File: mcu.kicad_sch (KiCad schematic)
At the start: 61 parts, among them J10 Micro_SD_Card, J11 Conn_01x06, J12 Conn_01x02, J13 USB_B, J14 USB_B, J8 Conn_02x05_Odd_Even, J9 Conn_01x06, SW1 SW_Push, SW2 SW_Push, U24 REF3333, U25 LPS25HB, U26 STM32F427ZGTx, U27 USBLC6-2SC6, Y1 8MHz

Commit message: update
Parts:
- removed J13: USB_B, conn_5_2.5mm:conn_5_2.5mm, symbol Connector_Generic:Conn_01x05
- removed J9: Conn_01x06, Connector:Tag-Connect_TC2030-IDC-NL_2x03_P1.27mm_Vertical, symbol Connector_Generic:Conn_01x06
- J12: footprint Connector_PinHeader_2.54mm:PinHeader_1x02_P2.54mm_Vertical -> Connector_PinHeader_2.54mm:PinHeader_1x04_P2.54mm_Vertical; symbol Connector_Generic:Conn_01x02 -> Connector_Generic:Conn_01x04
- J8: footprint Connector_PinHeader_1.27mm:PinHeader_2x05_P1.27mm_Vertical_SMD -> Connector_PinHeader_2.54mm:PinHeader_2x05_P2.54mm_Vertical
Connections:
- net +3V3: now also J12.1 (Pin_1)
- net GND: now also J12.4 (Pin_4)
- net UART_RX: now also J12.3 (Pin_3); no longer J12.2 (Pin_2)
- net UART_TX: now also J12.2 (Pin_2); no longer J12.1 (Pin_1)
- net AV10: now reaches U26.41 (PA5)
- net AV11: now reaches U26.42 (PA6)
- net AT3: now reaches U26.46 (PB0)
- net AT4: now reaches U26.47 (PB1)
- net LS17: now reaches U26.56 (PG0)
- net LS18: now reaches U26.57 (PG1)
- no-connect marks 31 -> 30
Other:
- note added: "1.3V @ 12V"
- note removed: "Pin header"
- note removed: "Tag Connect Debug Header"

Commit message: Updates - Route digital inputs to connector - Add optional VR conditioner - Second Enable for H-Bridge
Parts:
- D12, D13, D14, D15, D16: footprint LED_SMD:LED_0603_1608Metric_Castellated -> LED_SMD:LED_0603_1608Metric
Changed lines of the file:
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@@
       (effects (font (size 1.27 1.27)))
     )
-    (property "Footprint" "LED_SMD:LED_0603_1608Metric_Castellated" (at 211.455 173.99 0)
+    (property "Footprint" "LED_SMD:LED_0603_1608Metric" (at 211.455 173.99 0)
       (effects (font (size 1.27 1.27)) hide)
     )
@@
       (effects (font (size 1.27 1.27)))
     )
-    (property "Footprint" "LED_SMD:LED_0603_1608Metric_Castellated" (at 211.455 184.15 0)
+    (property "Footprint" "LED_SMD:LED_0603_1608Metric" (at 211.455 184.15 0)
       (effects (font (size 1.27 1.27)) hide)
     )
@@
       (effects (font (size 1.27 1.27)))
     )
-    (property "Footprint" "LED_SMD:LED_0603_1608Metric_Castellated" (at 211.455 193.675 0)
+    (property "Footprint" "LED_SMD:LED_0603_1608Metric" (at 211.455 193.675 0)
       (effects (font (size 1.27 1.27)) hide)
     )
@@
       (effects (font (size 1.27 1.27)))
     )
-    (property "Footprint" "LED_SMD:LED_0603_1608Metric_Castellated" (at 211.455 203.2 0)
+    (property "Footprint" "LED_SMD:LED_0603_1608Metric" (at 211.455 203.2 0)
       (effects (font (size 1.27 1.27)) hide)
     )
@@
       (effects (font (size 1.27 1.27)))
     )
-    (property "Footprint" "LED_SMD:LED_0603_1608Metric_Castellated" (at 211.455 212.725 0)
-      (effects (font (size 1.27 1.27)) hide)
-    )
+    (property "Footprint" "LED_SMD:LED_0603_1608Metric" (at 211.455 212.725 0)
+      (effects (font (size 1.27 1.27)) hide)
+    )

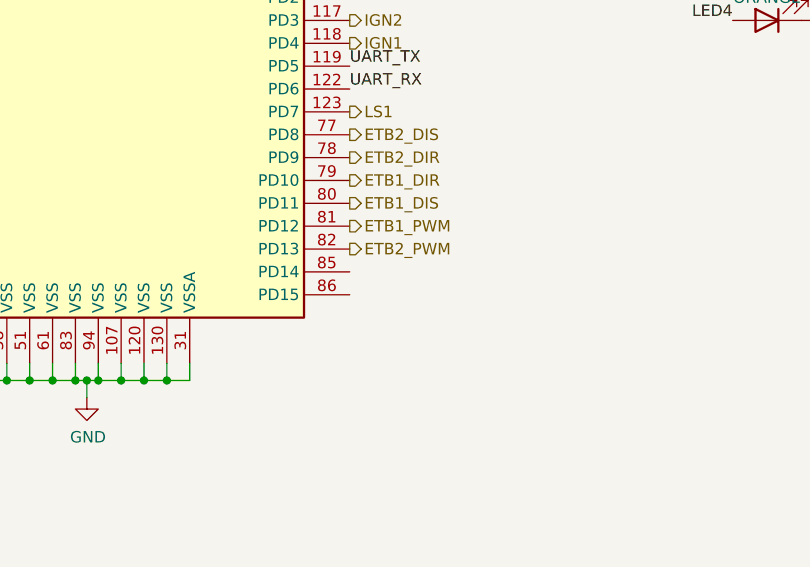
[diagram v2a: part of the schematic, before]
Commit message: Added ETB1_VSO and ETB1_ERR
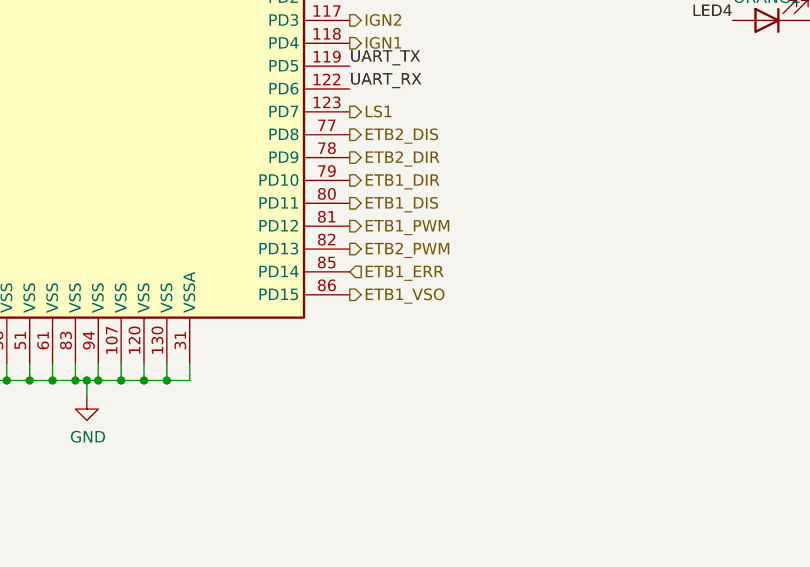
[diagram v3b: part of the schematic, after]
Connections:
- net ETB1_ERR: now reaches U26.85 (PD14)
- net ETB1_VSO: now reaches U26.86 (PD15)
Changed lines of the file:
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@@
+    (effects (font (size 1.27 1.27)) (justify left))
+  )
+  (hierarchical_label "ETB1_VSO" (shape output) (at 165.1 243.205 0) (fields_autoplaced)
     (effects (font (size 1.27 1.27)) (justify left))
   )
@@
     (effects (font (size 1.27 1.27)) (justify left))
   )
+  (hierarchical_label "ETB1_ERR" (shape input) (at 165.1 240.665 0) (fields_autoplaced)
+    (effects (font (size 1.27 1.27)) (justify left))
+  )
